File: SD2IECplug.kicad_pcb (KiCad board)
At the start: 2 copper layers, 50 x 49 mm, 45 parts, among them J1 ISP, J2 X6, J3 Aux, J4 IEC, J5 C64-CassettePort, J6 C64-CassettePort, J7 Power, J8 X3, Q1 IRLML2803, Q2 IRLML2803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

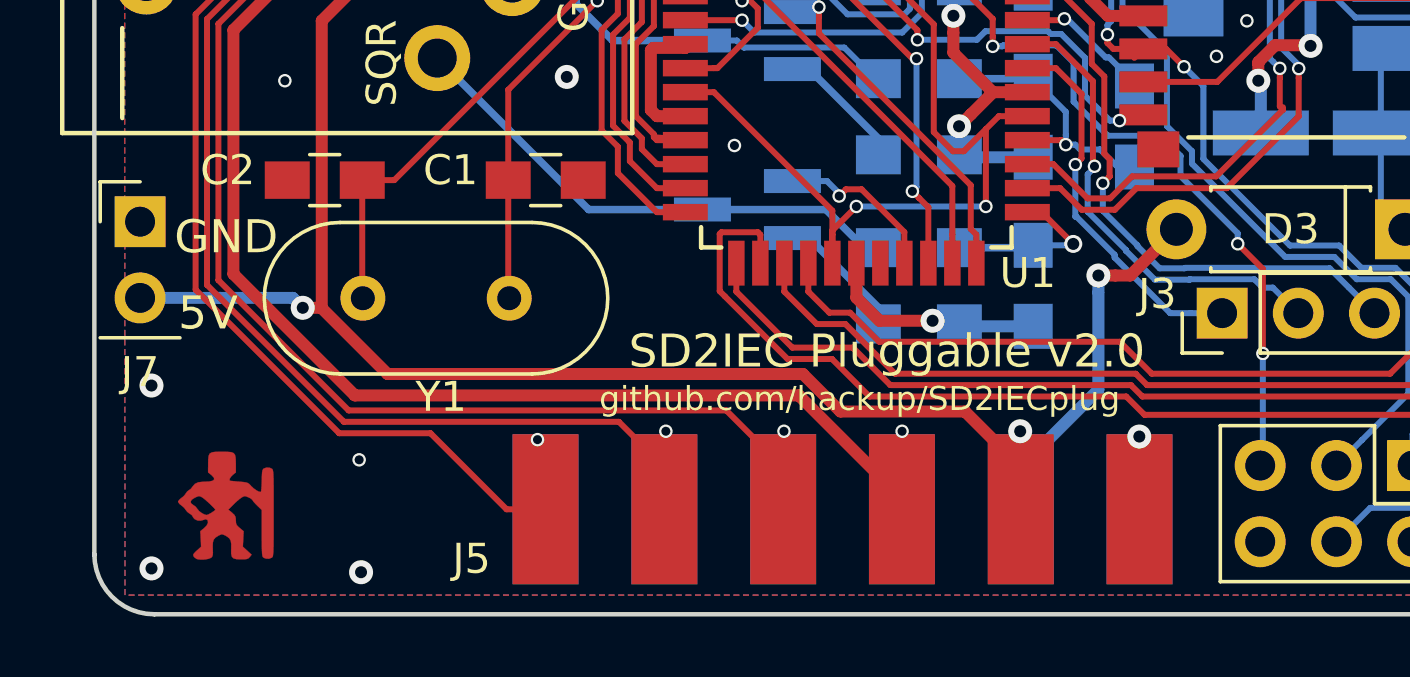
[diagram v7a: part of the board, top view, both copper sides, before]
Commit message: Aligned external power connector.
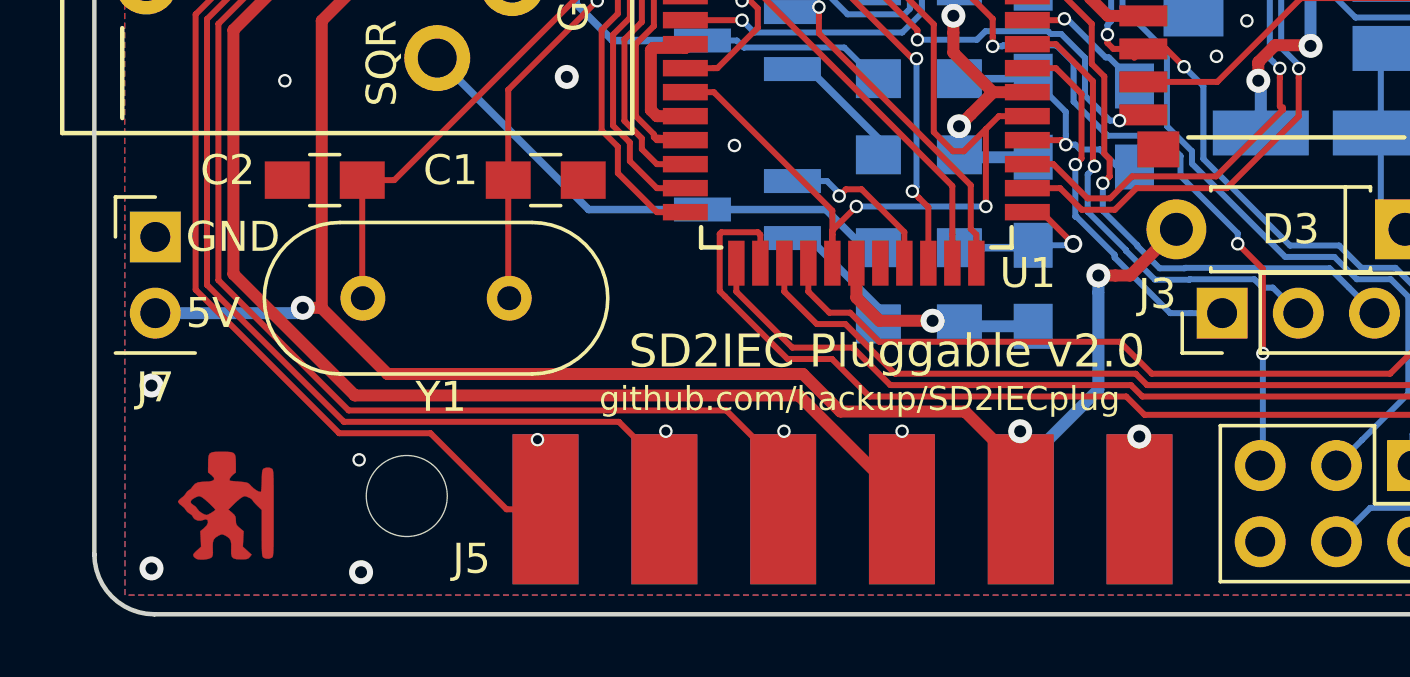
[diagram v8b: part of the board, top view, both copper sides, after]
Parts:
- added MH4: MountingHole, Mounting_Holes:MountingHole_2.7mm_M2.5, F.Cu at (68.4, 136.1)
- moved J7 0.72 mm to (60.0, 127.4)
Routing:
- net Cas-5V: track 100.2 -> 99.6 mm
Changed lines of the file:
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@@
     (thickness 1.6)
     (drawings 37)
-    (tracks 817)
+    (tracks 816)
     (zones 0)
-    (modules 45)
+    (modules 46)
     (nets 57)
   )
@@
   (title_block
     (title "SD2IEC Pluggable")
-    (date 2017-11-23)
-    (rev 0.9)
+    (date 2018-09-12)
+    (rev 2.0)
     (company www.hackup.net)
   )
@@
     (40 Dwgs.User user)
     (41 Cmts.User user)
-    (42 Eco1.User user)
+    (42 Eco1.User user hide)
     (43 Eco2.User user)
     (44 Edge.Cuts user)
@@
     (pad_drill 2.7)
     (pad_to_mask_clearance 0.2)
-    (aux_axis_origin 58 53)
-    (grid_origin 58 53)
+    (aux_axis_origin 105.752 104.562)
+    (grid_origin 105.752 104.562)
     (visible_elements 7FFFFFFF)
     (pcbplotparams
@@
   )
   (module Pin_Headers:Pin_Header_Straight_1x02_Pitch2.54mm (layer F.Cu)
-    (at 59.524 126.914)
+    (at 60.032 127.422)
     (descr "Through hole straight pin header, 1x02, 2.54mm pitch, single row")
     (tags "Through hole pin header THT 1x02 2.54mm single row")
@@
     (pad 1 np_thru_hole circle (at 0 0) (size 2.7 2.7) (drill 2.7) (layers *.Cu *.Mask))
   )
-  (gr_text GND (at 60.667 127.422) (layer F.SilkS)
-    (effects (font (size 1.1 1.1) (thickness 0.2)) (justify left))
-  )
-  (gr_text 5V (at 60.794 129.962) (layer F.SilkS)
-    (effects (font (size 1.1 1.1) (thickness 0.2)) (justify left))
+  (module Mounting_Holes:MountingHole_2.7mm_M2.5 (layer F.Cu)
+    (at 68.414 136.058)
+    (descr "Mounting Hole 2.7mm, no annular, M2.5")
+    (tags "mounting hole 2.7mm no annular m2.5")
+    (attr virtual)
+    (fp_text reference MH4 (at -0.127 0.127) (layer F.SilkS) hide
+      (effects (font (size 1 1) (thickness 0.15)))
+    )
+    (fp_text value MountingHole (at 0 -0.127) (layer F.Fab)
+      (effects (font (size 1 1) (thickness 0.15)))
+    )
+    (fp_text user %R (at 0.3 0) (layer F.Fab)
+      (effects (font (size 1 1) (thickness 0.15)))
+    )
+    (fp_circle (center 0 0) (end 2.7 0) (layer Cmts.User) (width 0.15))
+    (fp_circle (center 0 0) (end 2.95 0) (layer F.CrtYd) (width 0.05))
+    (pad 1 np_thru_hole circle (at 0 0) (size 2.7 2.7) (drill 2.7) (layers *.Cu *.Mask))
+  )
+  (gr_text GND (at 61.048 127.422) (layer F.SilkS)
+    (effects (font (size 1 1) (thickness 0.2)) (justify left))
+  )
+  (gr_text 5V (at 61.048 129.962) (layer F.SilkS)
+    (effects (font (size 1 1) (thickness 0.2)) (justify left))
   )
   (gr_text github.com/hackup/SD2IECplug (at 74.8275 132.8195) (layer F.SilkS)
@@
   (gr_arc (start 60 104.354) (end 58 104.354) (angle 90) (layer Edge.Cuts) (width 0.15))
   (gr_text "SD2IEC Pluggable v2.0" (at 84.416 131.232) (layer F.SilkS)
-    (effects (font (size 1.1 1.1) (thickness 0.2)))
+    (effects (font (size 1.1 1.1) (thickness 0.22)))
   )
   (gr_arc (start 60 138) (end 60 140) (angle 90) (layer Edge.Cuts) (width 0.15))
@@
   (gr_line (start 58 140.078) (end 58 90.338) (angle 90) (layer Eco1.User) (width 0.2))
   (gr_line (start 108.038 90.338) (end 108.038 140.122) (angle 90) (layer Eco1.User) (width 0.2))
+  (via (at 74.256 105.705) (size 0.8) (drill 0.4) (layers F.Cu B.Cu) (net 0))
   (via (at 74.764 119.548) (size 0.45) (drill 0.3) (layers F.Cu B.Cu) (net 1))
   (segment (start 71.796 122.516) (end 71.796 125.528) (width 0.2) (layer F.Cu) (net 1))
@@
   (via (at 59.9685 113.96) (size 0.45) (drill 0.3) (layers F.Cu B.Cu) (net 25))
   (via (at 64.35 122.215) (size 0.45) (drill 0.3) (layers F.Cu B.Cu) (net 25))
-  (via (at 74.256 105.705) (size 0.8) (drill 0.4) (layers F.Cu B.Cu) (net 0))
   (via (at 71.4 104.8) (size 0.8) (drill 0.4) (layers F.Cu B.Cu) (net 25))
   (via (at 68 108.6) (size 0.8) (drill 0.4) (layers F.Cu B.Cu) (net 25))
@@
   (segment (start 88.968 96.942) (end 88.88 96.854) (width 0.4) (layer F.Cu) (net 26))
   (segment (start 90.131 96.942) (end 88.968 96.942) (width 0.4) (layer F.Cu) (net 26))
-  (segment (start 59.524 129.454) (end 62.188998 129.454) (width 0.4) (layer B.Cu) (net 26))
   (segment (start 65.580001 129.797003) (end 65.580001 120.215997) (width 0.4) (layer F.Cu) (net 26))
   (segment (start 88.88 135.1) (end 91.467741 132.512259) (width 0.4) (layer B.Cu) (net 26))
@@
   (segment (start 82.869577 133.241032) (end 81.619434 131.990889) (width 0.4) (layer F.Cu) (net 26))
   (via (at 64.9469 129.7842) (size 0.8) (drill 0.4) (layers F.Cu B.Cu) (net 26))
-  (segment (start 62.188998 129.454) (end 64.6167 129.454) (width 0.4) (layer B.Cu) (net 26))
-  (segment (start 64.6167 129.454) (end 64.9469 129.7842) (width 0.4) (layer B.Cu) (net 26))
   (segment (start 65.567198 129.7842) (end 65.580001 129.797003) (width 0.4) (layer F.Cu) (net 26))
   (segment (start 64.9469 129.7842) (end 65.567198 129.7842) (width 0.4) (layer F.Cu) (net 26))
+  (segment (start 64.7691 129.962) (end 64.9469 129.7842) (width 0.4) (layer B.Cu) (net 26))
+  (segment (start 60.032 129.962) (end 64.7691 129.962) (width 0.4) (layer B.Cu) (net 26))
   (via (at 84.924 133.899) (size 0.45) (drill 0.3) (layers F.Cu B.Cu) (net 27))
   (segment (start 84.92 136.5) (end 84.92 133.903) (width 0.2) (layer B.Cu) (net 27))
